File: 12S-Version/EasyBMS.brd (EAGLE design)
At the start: 49 x 100 mm, 155 parts, among them IC1 LM2596S-5.0_NOPB, IC2 LTC6811IG-1#PBF, Q10 BSS84LT1G, Q11 BSS84LT1G, Q12 BSS84LT1G, Q13 BSS84LT1G, Q2 BSS84LT1G, Q3 BSS84LT1G, Q4 BSS84LT1G, Q5 BSS84LT1G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

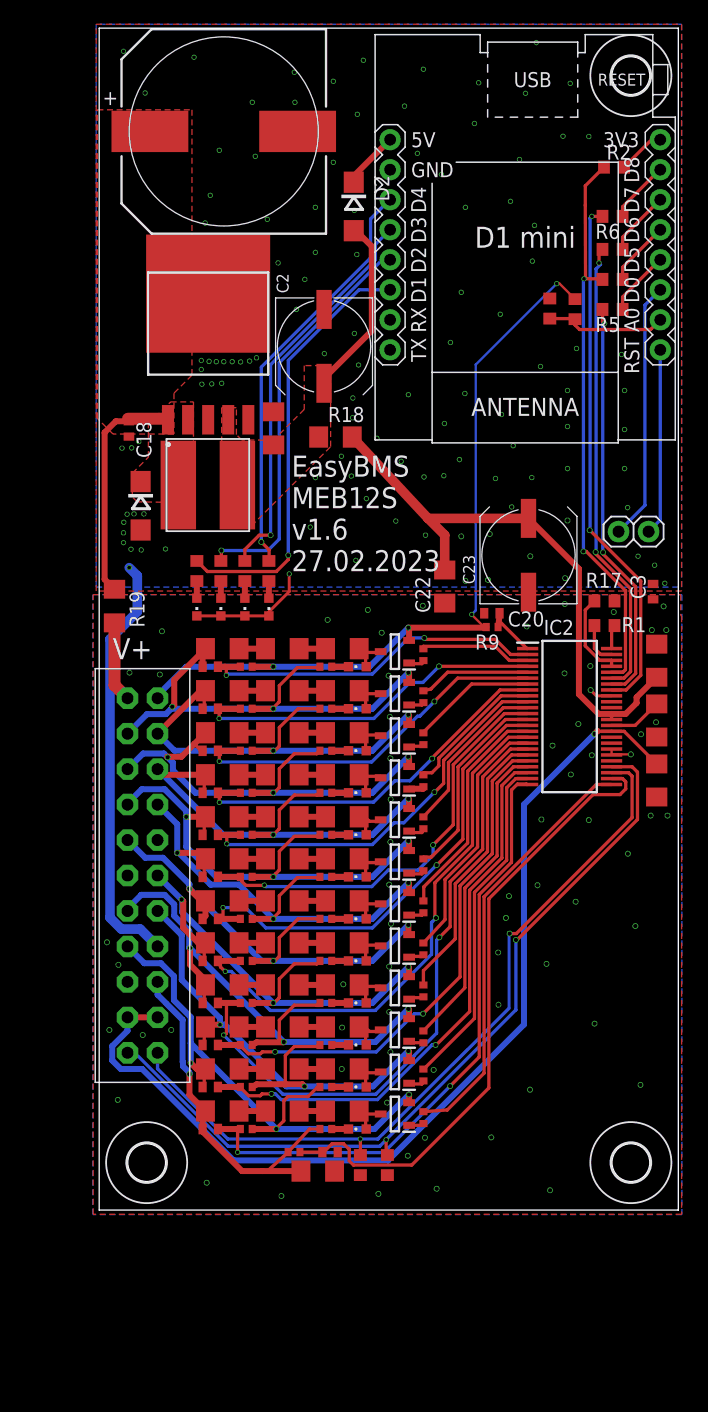
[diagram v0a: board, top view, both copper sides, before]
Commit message: pinheader for display added
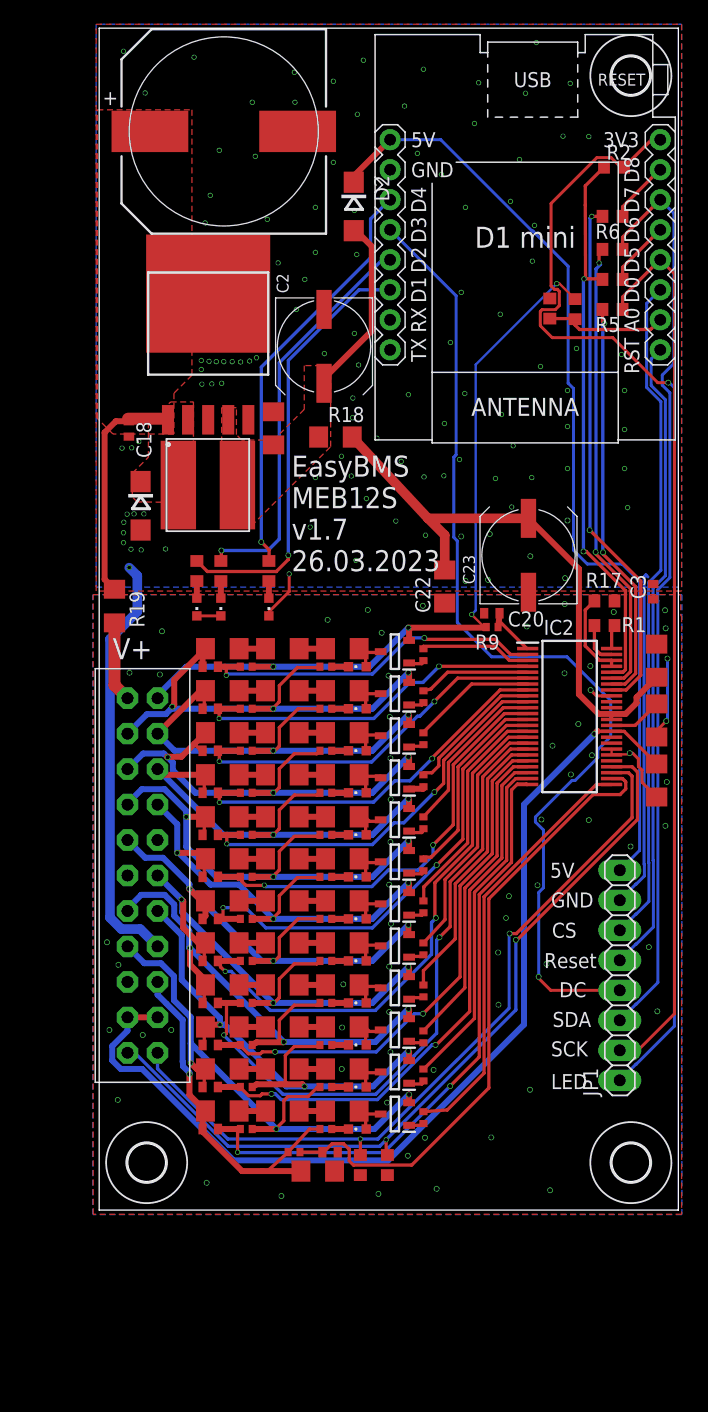
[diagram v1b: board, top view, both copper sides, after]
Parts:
- removed JP3: (no value), pinhead_own:1X02
- removed LED3: KT-0603R, led:CHIPLED_0603
- removed R55: 200R0, rcl:R0603
- added JP1: (no value), pinhead:1X08
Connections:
- removed net N$119: R62.1, U$2.JP1.6
- removed net N$120: R55.2, U$2.JP2.5
- removed net N$25: D2.C, U$2.JP2.8
- removed net N$5: JP3.2, U$2.JP1.1
- removed net N$6: JP3.1, U$2.JP1.3
- removed net N$7: R5.1, U$2.JP1.4
- new net 5VINESP: D2.C, JP1.8, U$2.JP2.8
- new net D0: JP1.6, U$2.JP1.3
- new net D3: JP1.4, U$2.JP2.5
- new net MOSIESP: JP1.3, R62.1, U$2.JP1.6
- new net RESET: JP1.5, U$2.JP1.1
- new net SCKESP: JP1.2, R5.1, U$2.JP1.4
- net +3V3: now also JP1.1
- net GND: now also JP1.7; no longer LED1.C, LED2.C, LED3.C
- net N$3: now also LED1.C, LED2.C; no longer LED3.A, R55.1
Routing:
- net +3V3: track 4.02 -> 98.3 mm, vias 0 -> 1
- net D3: track 0.00 -> 85.5 mm, vias 0 -> 1
- net 5VINESP: track 0.00 -> 80.4 mm
- net MOSIESP: track 0.00 -> 77.9 mm
- net SCKESP: track 0.00 -> 75.7 mm
- net D0: track 0.00 -> 56.6 mm
- net RESET: track 0.00 -> 54.1 mm
- net N$120: track 33.7 -> 0.00 mm, vias 1 -> 0
- net GND: track 46.2 -> 68.9 mm, vias 113 -> 110
- net N$6: track 21.9 -> 0.00 mm
- net N$5: track 15.8 -> 0.00 mm
- net GND2: track 4.52 -> 15.9 mm, vias 68 -> 65
- net N$7: track 5.55 -> 0.00 mm
- net N$119: track 5.53 -> 0.00 mm
- net N$25: track 4.87 -> 0.00 mm
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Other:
- board text added: "5V"
- board text added: "CS"
- board text added: "DC"
- board text added: "EasyBMS MEB12S v1.7 26.03.2023"
- board text added: "GND"
- board text added: "LED"
- board text added: "Reset"
- board text added: "SCK"
- board text added: "SDA"
- board text removed: "EasyBMS MEB12S v1.6 27.02.2023"

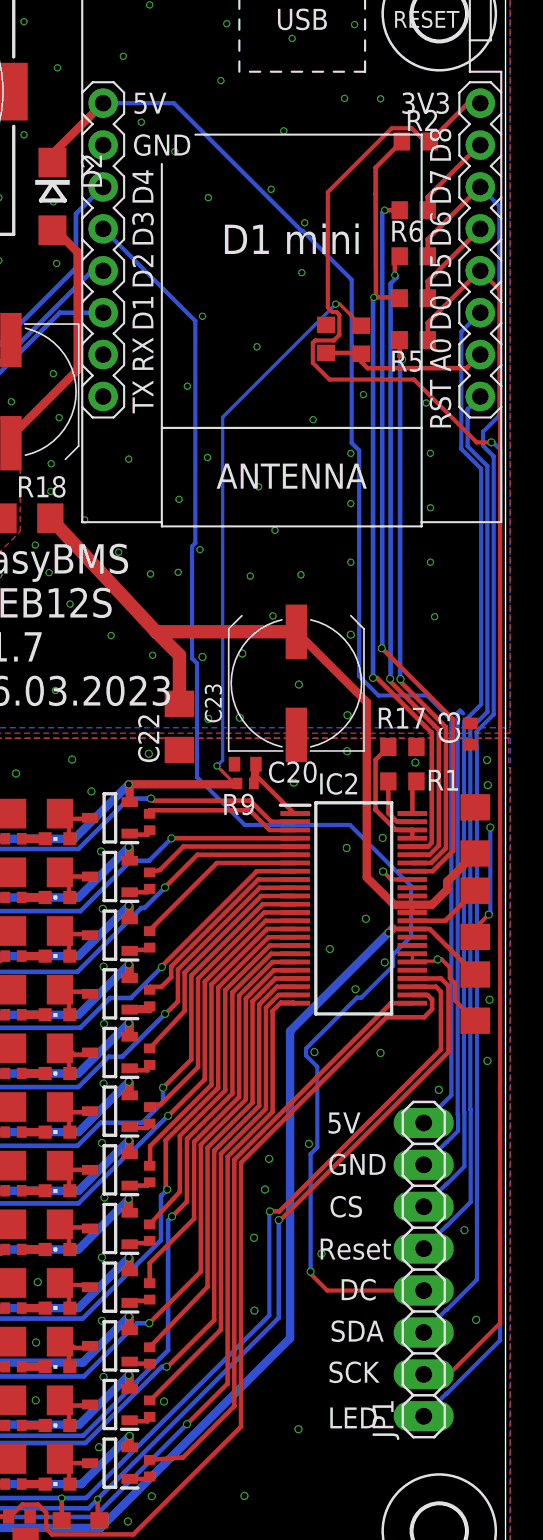
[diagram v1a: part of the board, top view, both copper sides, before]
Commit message: moved display connector
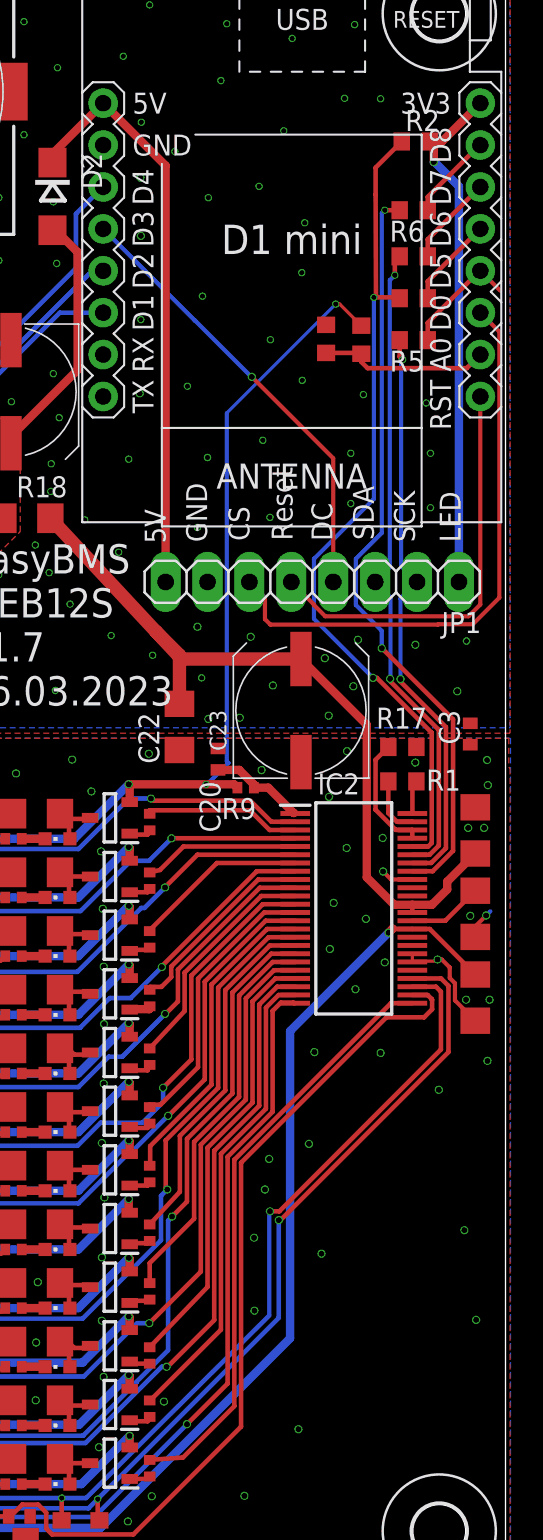
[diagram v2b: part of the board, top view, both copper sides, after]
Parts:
- moved JP1 42.2 mm to (37.3, 61.5), turned to 180 degrees
- moved C20 1.68 mm to (31.6, 50.8), turned to 270 degrees
- moved C23 1.67 mm to (36.6, 53.7)
- moved R9 0.25 mm to (33.2, 49.1)
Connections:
- net MOSI: now also JP1.3
- net MOSIESP: no longer JP1.3
- net SCK: now also JP1.2
- net SCKESP: no longer JP1.2
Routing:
- net MOSIESP: track 77.9 -> 5.53 mm
- net SCKESP: track 75.7 -> 7.24 mm
- net +3V3: track 98.3 -> 31.8 mm
- net D3: track 85.5 -> 27.3 mm
- net 5VINESP: track 80.4 -> 35.5 mm
- net RESET: track 54.1 -> 25.2 mm
- net GND: track 68.9 -> 40.1 mm, vias 110 -> 111
- net D0: track 56.6 -> 35.4 mm
- net GND2: track 15.9 -> 10.9 mm, vias 65 -> 70
- net MISO: track 47.7 -> 50.7 mm
- net CSB: track 44.6 -> 45.9 mm
- net V+: track 5.14 -> 5.98 mm
- net SCK: track 34.5 -> 35.3 mm
- net +5V: track 48.8 -> 48.1 mm
- net MOSI: track 39.1 -> 39.8 mm

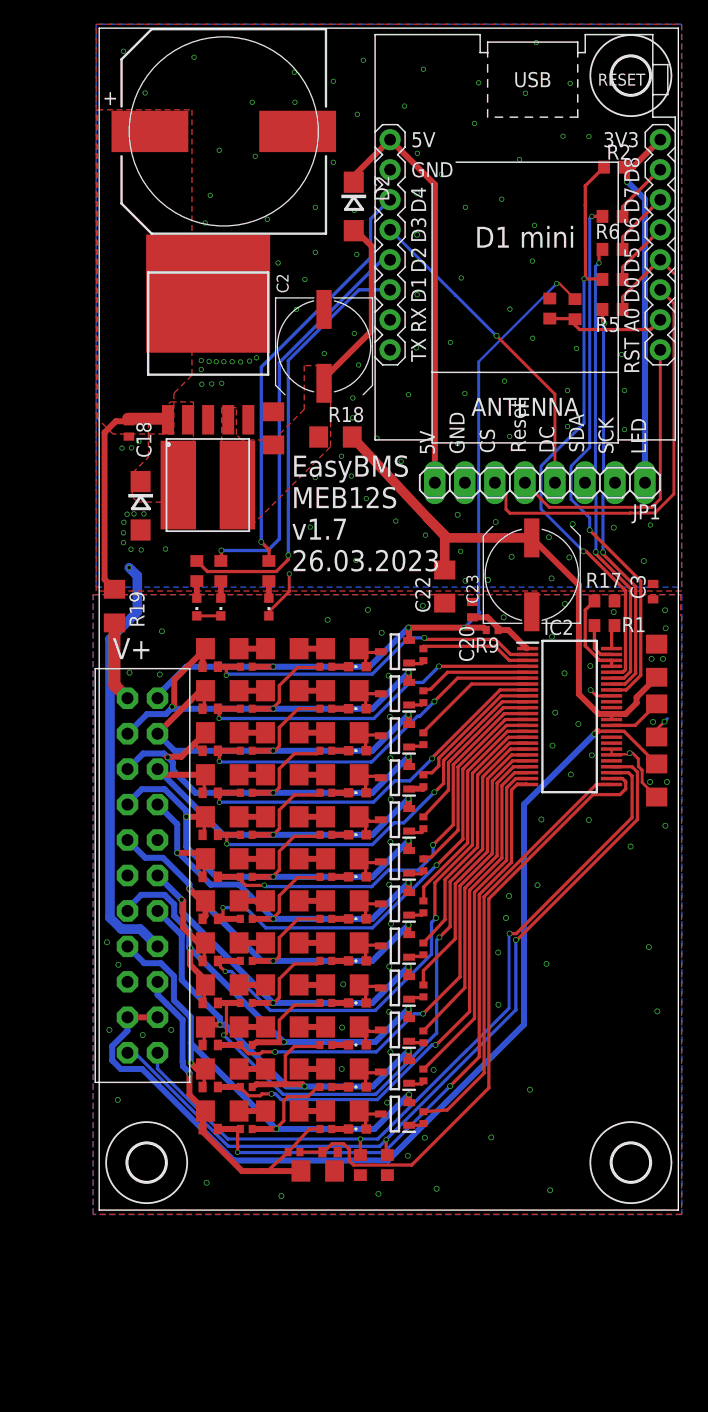
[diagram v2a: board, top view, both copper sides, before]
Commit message: thermals added for THT pins
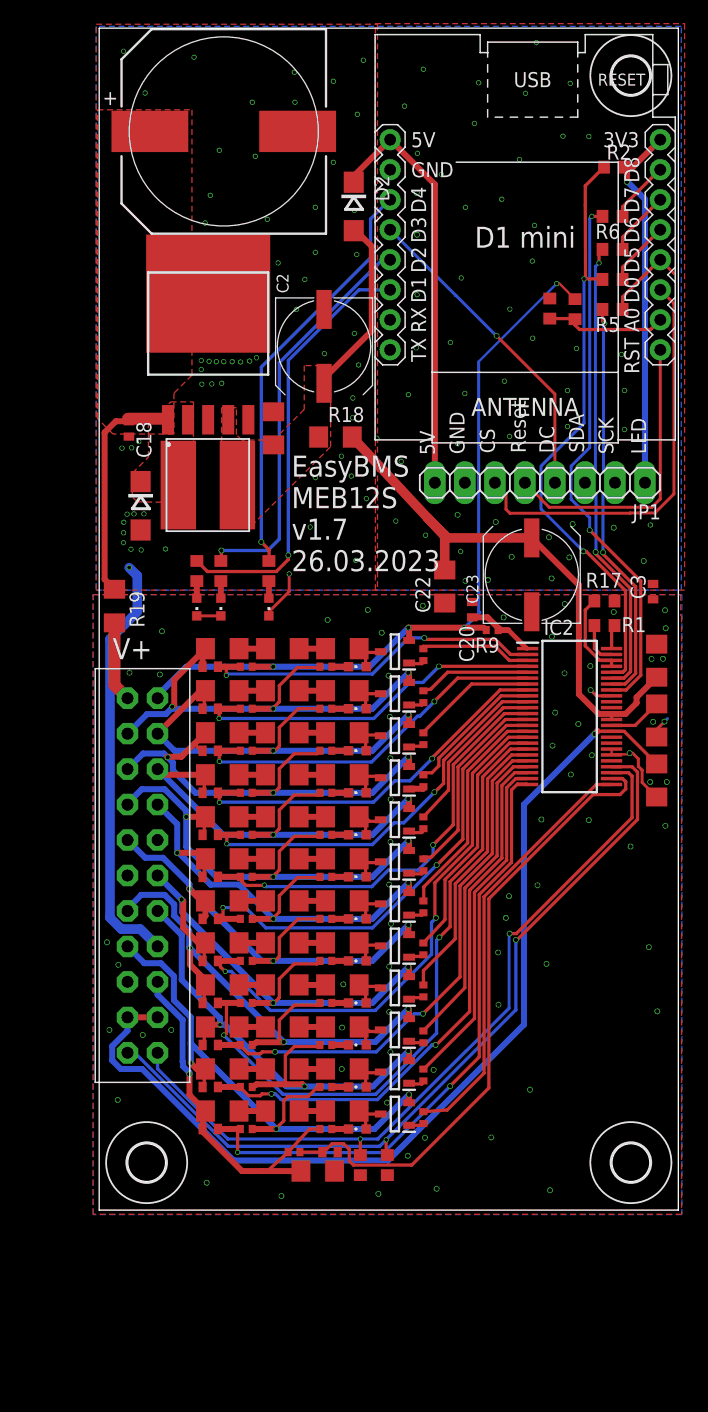
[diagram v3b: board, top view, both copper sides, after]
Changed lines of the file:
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@@
 <drawing>
 <settings>
-<setting alwaysvectorfont="yes"/>
+<setting alwaysvectorfont="no"/>
 <setting verticaltext="up"/>
 </settings>
@@
 <signal name="GND">
 <contactref element="R16" pad="1"/>
-<polygon width="0.127" layer="16" isolate="0.4" thermals="no">
-<vertex x="-0.254" y="52.705"/>
-<vertex x="49.276" y="52.705"/>
-<vertex x="49.276" y="100.33"/>
-<vertex x="-0.254" y="100.33"/>
+<polygon width="0.127" layer="16" isolate="0.4">
+<vertex x="-0.254" y="52.451"/>
+<vertex x="49.2506" y="52.451"/>
+<vertex x="49.2506" y="100.1522"/>
+<vertex x="-0.254" y="100.1522"/>
 </polygon>
 <polygon width="0.127" layer="1" isolate="0.4" thermals="no" rank="3">
 <vertex x="-0.254" y="100.33"/>
-<vertex x="49.276" y="100.33"/>
-<vertex x="49.276" y="52.3748"/>
-<vertex x="-0.254" y="52.3748"/>
+<vertex x="23.5458" y="100.33"/>
+<vertex x="23.5458" y="52.451"/>
+<vertex x="-0.254" y="52.451"/>
 </polygon>
 <via x="27.6098" y="57.0992" extent="1-16" drill="0.3"/>
@@
 <via x="26.8224" y="72.9742" extent="1-16" drill="0.35"/>
 <via x="43.5356" y="57.7342" extent="1-16" drill="0.35"/>
+<polygon width="0.127" layer="1" isolate="0.4" rank="3">
+<vertex x="23.368" y="100.3808"/>
+<vertex x="49.53" y="100.3808"/>
+<vertex x="49.53" y="52.451"/>
+<vertex x="23.368" y="52.451"/>
+</polygon>
 </signal>
 <signal name="N$202">
@@
 <signal name="SCK">
 <contactref element="R5" pad="2"/>
-<wire x1="42.672" y1="74.93" x2="42.6085" y2="74.93" width="0.2794" layer="16"/>
-<wire x1="42.672" y1="74.93" x2="42.760803125" y2="75.018803125" width="0.2794" layer="16"/>
 <via x="42.760803125" y="75.018803125" extent="1-16" drill="0.3"/>
-<wire x1="42.760803125" y1="75.018803125" x2="42.584" y2="75.19560625" width="0.2794" layer="1"/>
-<wire x1="42.584" y1="75.19560625" x2="42.584" y2="76.2" width="0.2794" layer="1"/>
 <via x="42.63455625" y="55.6514" extent="1-16" drill="0.35"/>
 <wire x1="45.3898" y1="52.7412375" x2="45.3898" y2="45.4043625" width="0.2794" layer="1"/>
@@
 <wire x1="43.6372" y1="61.5442" x2="43.6245" y2="61.5442" width="0.254" layer="16"/>
 <wire x1="43.6372" y1="61.5442" x2="42.672" y2="62.5094" width="0.254" layer="16"/>
-<wire x1="42.672" y1="62.5094" x2="42.672" y2="74.93" width="0.254" layer="16"/>
+<wire x1="42.672" y1="62.5094" x2="42.672" y2="74.7522" width="0.254" layer="16"/>
+<wire x1="42.584" y1="76.2" x2="42.584" y2="75.19560625" width="0.254" layer="1"/>
+<wire x1="42.584" y1="75.19560625" x2="42.760803125" y2="75.018803125" width="0.254" layer="1"/>
+<wire x1="42.672" y1="74.7522" x2="42.672" y2="74.93" width="0.254" layer="16"/>
+<wire x1="42.672" y1="74.93" x2="42.760803125" y2="75.018803125" width="0.254" layer="16"/>
 </signal>
 <signal name="CSB">
@@
 <wire x1="36.1854" y1="47.5076" x2="36.2518" y2="47.5076" width="0.2794" layer="1"/>
 <wire x1="33.7486" y1="49.0728" x2="34.6202" y2="49.0728" width="0.508" layer="1"/>
-<wire x1="34.6202" y1="49.0728" x2="36.1544" y2="47.5386" width="0.508" layer="1"/>
-<wire x1="36.1544" y1="47.5386" x2="36.1854" y2="47.5386" width="0.508" layer="1"/>
 <wire x1="33.7486" y1="49.2616125" x2="33.7486" y2="49.0728" width="0.508" layer="1"/>
 <wire x1="33.7486" y1="49.2616125" x2="32.8602125" y2="50.15" width="0.508" layer="1"/>
 <wire x1="31.5722" y1="50.15" x2="32.8602125" y2="50.15" width="0.508" layer="1"/>
-<wire x1="36.1854" y1="47.5386" x2="36.1854" y2="47.5076" width="0" layer="19" extent="1-1"/>
+<wire x1="34.6202" y1="49.0728" x2="36.1854" y2="47.5076" width="0.4064" layer="1"/>
 </signal>
 <signal name="C12+">
@@
 <wire x1="38.7096" y1="78.3844" x2="32.1056" y2="71.7804" width="0.2" layer="16"/>
 <wire x1="4.936" y1="43.308" x2="4.936" y2="43.544" width="0.2" layer="16"/>
-<wire x1="32.5454" y1="49.276" x2="32.7486" y2="49.0728" width="0.508" layer="1"/>
-<wire x1="26.162" y1="49.276" x2="32.5454" y2="49.276" width="0.508" layer="1"/>
+<wire x1="32.5454" y1="49.276" x2="30.861" y2="49.276" width="0.508" layer="1"/>
+<wire x1="30.861" y1="49.276" x2="26.162" y2="49.276" width="0.508" layer="1"/>
 <wire x1="32.1056" y1="71.7804" x2="32.1056" y2="50.673" width="0.254" layer="16"/>
 <wire x1="32.1056" y1="50.673" x2="32.2072" y2="50.5714" width="0.254" layer="16"/>
 <wire x1="32.2072" y1="50.5714" x2="30.9118" y2="49.276" width="0.254" layer="16"/>
 <wire x1="30.9118" y1="49.276" x2="30.854" y2="49.276" width="0.254" layer="16"/>
-<wire x1="32.7486" y1="49.0728" x2="30.854" y2="49.276" width="0" layer="19" extent="1-1"/>
+<wire x1="32.7486" y1="49.0728" x2="32.5454" y2="49.276" width="0.4064" layer="1"/>
+<wire x1="30.854" y1="49.276" x2="30.861" y2="49.276" width="0.4064" layer="1"/>
 </signal>
 <signal name="C11+">
